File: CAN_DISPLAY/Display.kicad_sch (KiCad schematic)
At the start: 14 parts, among them J1 DISPLAY, J14 Display, J2 I2C Sensor 1, J3 I2C Sensor 2, U6 BME280

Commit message: PCB Fixes
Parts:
- added J16: BME280 Module, Connector_PinHeader_2.54mm:PinHeader_1x04_P2.54mm_Vertical, symbol Connector_Generic:Conn_01x04
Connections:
- net +3V3: now also J16.1 (Pin_1)
- net GND: now also J16.2 (Pin_2)
- net I2C_SCL: now also J16.3 (Pin_3)
- net I2C_SDA: now also J16.4 (Pin_4)
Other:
- moved on the sheet: C4, C5, J2, J3

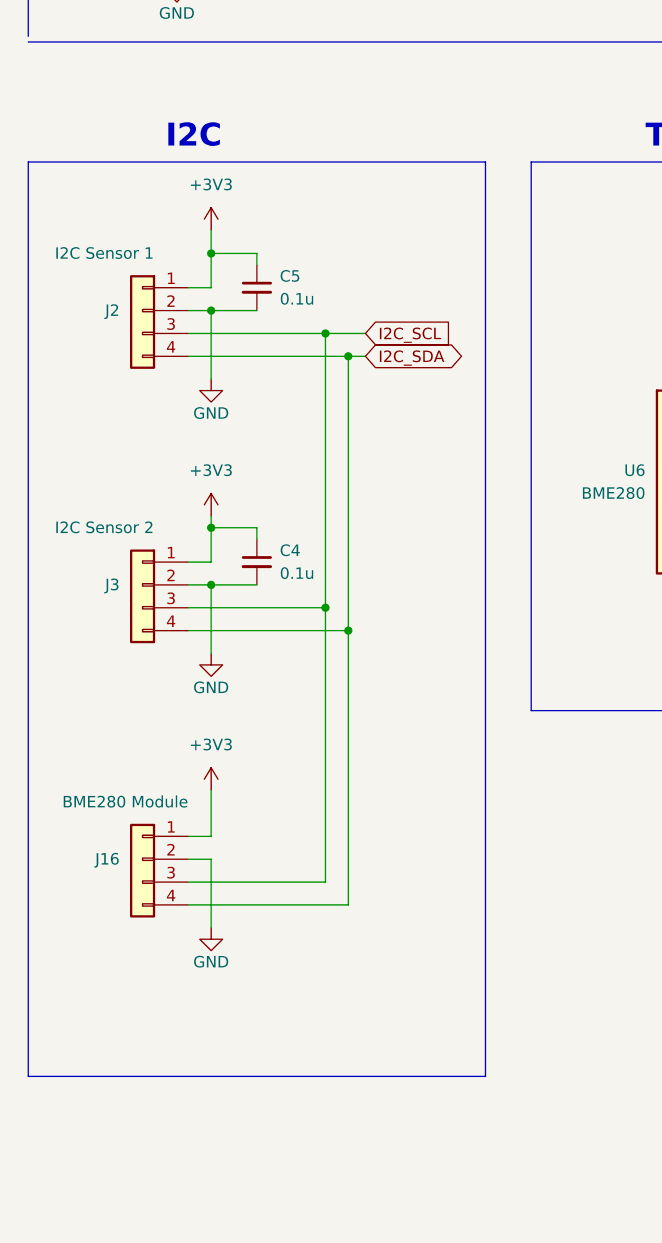
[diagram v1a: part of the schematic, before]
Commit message: Add Ambient Light
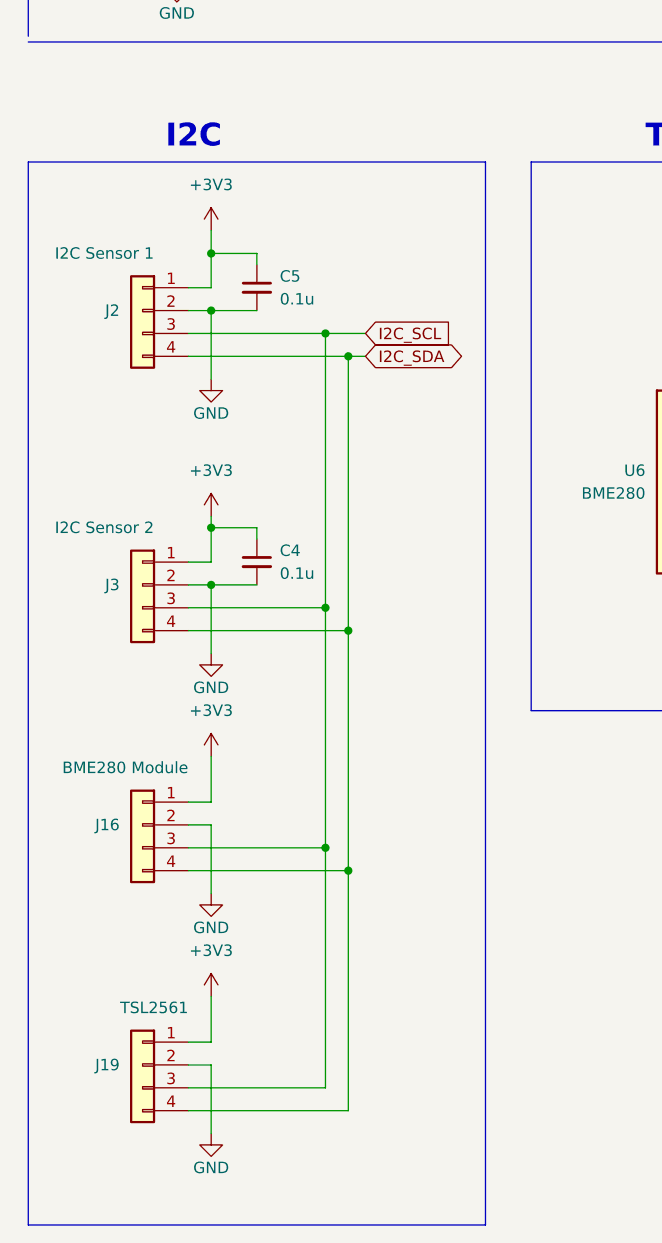
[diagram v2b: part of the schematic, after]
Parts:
- added J19: TSL2561, Connector_PinHeader_2.54mm:PinHeader_1x04_P2.54mm_Vertical, symbol Connector_Generic:Conn_01x04
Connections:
- net +3V3: now also J19.1 (Pin_1)
- net GND: now also J19.2 (Pin_2)
- net I2C_SCL: now also J19.3 (Pin_3)
- net I2C_SDA: now also J19.4 (Pin_4)
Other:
- moved on the sheet: J16
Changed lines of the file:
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@@
   (junction (at 46.355 41.91) (diameter 0) (color 0 0 0 0)
   )
+  (junction (at 54.61 153.67) (diameter 0) (color 0 0 0 0)
+  )
   (junction (at 67.945 28.575) (diameter 0) (color 0 0 0 0)
   )
@@
   )
   (junction (at 54.61 127) (diameter 0) (color 0 0 0 0)
+  )
+  (junction (at 52.07 151.13) (diameter 0) (color 0 0 0 0)
   )
   (no_connect (at 33.02 44.45))
@@
     (stroke (width 0) (type default))
   )
-  (wire (pts (xy 39.37 160.02) (xy 39.37 152.4))
+  (wire (pts (xy 39.37 156.21) (xy 39.37 148.59))
     (stroke (width 0) (type default))
   )
@@
     (stroke (width 0) (type default))
   )
+  (wire (pts (xy 36.83 172.72) (xy 39.37 172.72))
+    (stroke (width 0) (type default))
+  )
   (wire (pts (xy 101.6 93.98) (xy 96.52 93.98))
     (stroke (width 0) (type default))
   )
-  (wire (pts (xy 52.07 124.46) (xy 52.07 154.94))
+  (wire (pts (xy 52.07 124.46) (xy 52.07 151.13))
     (stroke (width 0) (type default))
   )
@@
     (stroke (width 0) (type default))
   )
+  (wire (pts (xy 36.83 177.8) (xy 52.07 177.8))
+    (stroke (width 0) (type default))
+  )
   (wire (pts (xy 52.705 39.37) (xy 45.085 39.37))
     (stroke (width 0) (type default))
@@
     (stroke (width 0) (type default))
   )
-  (wire (pts (xy 36.83 149.86) (xy 39.37 149.86))
+  (wire (pts (xy 36.83 146.05) (xy 39.37 146.05))
     (stroke (width 0) (type default))
   )
@@
     (stroke (width 0) (type default))
   )
+  (wire (pts (xy 39.37 182.88) (xy 39.37 175.26))
+    (stroke (width 0) (type default))
+  )
   (wire (pts (xy 54.61 127) (xy 54.61 96.52))
     (stroke (width 0) (type default))
@@
     (stroke (width 0) (type default))
   )
+  (wire (pts (xy 39.37 175.26) (xy 36.83 175.26))
+    (stroke (width 0) (type default))
+  )
   (wire (pts (xy 39.37 121.92) (xy 44.45 121.92))
     (stroke (width 0) (type default))
@@
     (stroke (width 0) (type default))
   )
-  (wire (pts (xy 54.61 157.48) (xy 54.61 127))
+  (wire (pts (xy 54.61 153.67) (xy 54.61 127))
     (stroke (width 0) (type default))
   )
@@
     (stroke (width 0) (type default))
   )
-  (wire (pts (xy 39.37 144.78) (xy 39.37 149.86))
+  (wire (pts (xy 39.37 140.97) (xy 39.37 146.05))
+    (stroke (width 0) (type default))
+  )
+  (wire (pts (xy 39.37 167.64) (xy 39.37 172.72))
     (stroke (width 0) (type default))
   )
@@
     (stroke (width 0) (type default))
   )
+  (wire (pts (xy 36.83 180.34) (xy 54.61 180.34))
+    (stroke (width 0) (type default))
+  )
   (wire (pts (xy 33.02 34.29) (xy 35.56 34.29))
     (stroke (width 0) (type default))
@@
     (stroke (width 0) (type default))
   )
-  (wire (pts (xy 36.83 157.48) (xy 54.61 157.48))
+  (wire (pts (xy 36.83 153.67) (xy 54.61 153.67))
     (stroke (width 0) (type default))
   )
@@
     (stroke (width 0) (type default))
   )
-  (wire (pts (xy 36.83 154.94) (xy 52.07 154.94))
+  (wire (pts (xy 36.83 151.13) (xy 52.07 151.13))
     (stroke (width 0) (type default))
   )
@@
     (stroke (width 0) (type default))
   )
+  (wire (pts (xy 54.61 180.34) (xy 54.61 153.67))
+    (stroke (width 0) (type default))
+  )
   (wire (pts (xy 119.38 118.11) (xy 114.3 118.11))
     (stroke (width 0) (type default))
   )
-  (wire (pts (xy 39.37 152.4) (xy 36.83 152.4))
+  (wire (pts (xy 39.37 148.59) (xy 36.83 148.59))
+    (stroke (width 0) (type default))
+  )
+  (wire (pts (xy 52.07 151.13) (xy 52.07 177.8))
     (stroke (width 0) (type default))
   )
@@
     (fill (type none))
   )
-  (rectangle (start 19.05 74.93) (end 69.85 176.53)
+  (rectangle (start 19.05 74.93) (end 69.85 193.04)
     (stroke (width 0) (type default))
     (fill (type none))
@@
     )
   )
-  (symbol (lib_id "power:GND") (at 39.37 160.02 0) (mirror y) (unit 1)
-    (in_bom yes) (on_board yes) (dnp no)
-    (property "Reference" "#PWR086" (at 39.37 166.37 0)
-      (effects (font (size 1.27 1.27)) hide)
-    )
-    (property "Value" "GND" (at 39.37 163.83 0)
-      (effects (font (size 1.27 1.27)))
-    )
-    (property "Footprint" "" (at 39.37 160.02 0)
-      (effects (font (size 1.27 1.27)) hide)
-    )
-    (property "Datasheet" "" (at 39.37 160.02 0)
+  (symbol (lib_id "power:GND") (at 39.37 156.21 0) (mirror y) (unit 1)
+    (in_bom yes) (on_board yes) (dnp no)
+    (property "Reference" "#PWR086" (at 39.37 162.56 0)
+      (effects (font (size 1.27 1.27)) hide)
+    )
+    (property "Value" "GND" (at 39.37 160.02 0)
+      (effects (font (size 1.27 1.27)))
+    )
+    (property "Footprint" "" (at 39.37 156.21 0)
+      (effects (font (size 1.27 1.27)) hide)
+    )
+    (property "Datasheet" "" (at 39.37 156.21 0)
       (effects (font (size 1.27 1.27)) hide)
     )
@@
     )
   )
-  (symbol (lib_id "power:+3V3") (at 39.37 144.78 0) (unit 1)
+  (symbol (lib_id "power:+3V3") (at 39.37 140.97 0) (unit 1)
     (in_bom yes) (on_board yes) (dnp no) (fields_autoplaced)
-    (property "Reference" "#PWR085" (at 39.37 148.59 0)
-      (effects (font (size 1.27 1.27)) hide)
-    )
-    (property "Value" "+3V3" (at 39.37 139.7 0)
-      (effects (font (size 1.27 1.27)))
-    )
-    (property "Footprint" "" (at 39.37 144.78 0)
-      (effects (font (size 1.27 1.27)) hide)
-    )
-    (property "Datasheet" "" (at 39.37 144.78 0)
+    (property "Reference" "#PWR085" (at 39.37 144.78 0)
+      (effects (font (size 1.27 1.27)) hide)
+    )
+    (property "Value" "+3V3" (at 39.37 135.89 0)
+      (effects (font (size 1.27 1.27)))
+    )
+    (property "Footprint" "" (at 39.37 140.97 0)
+      (effects (font (size 1.27 1.27)) hide)
+    )
+    (property "Datasheet" "" (at 39.37 140.97 0)
       (effects (font (size 1.27 1.27)) hide)
     )
@@
     )
   )
-  (symbol (lib_id "Connector_Generic:Conn_01x04") (at 31.75 152.4 0) (mirror y) (unit 1)
-    (in_bom yes) (on_board yes) (dnp no)
-    (property "Reference" "J16" (at 29.21 152.4 0)
-      (effects (font (size 1.27 1.27)) (justify left))
-    )
-    (property "Value" "BME280 Module" (at 36.83 146.05 0)
-      (effects (font (size 1.27 1.27)) (justify left))
-    )
-    (property "Footprint" "Connector_PinHeader_2.54mm:PinHeader_1x04_P2.54mm_Vertical" (at 31.75 152.4 0)
-      (effects (font (size 1.27 1.27)) hide)
-    )
-    (property "Datasheet" "~" (at 31.75 152.4 0)
+  (symbol (lib_id "Connector_Generic:Conn_01x04") (at 31.75 148.59 0) (mirror y) (unit 1)
+    (in_bom yes) (on_board yes) (dnp no)
+    (property "Reference" "J16" (at 29.21 148.59 0)
+      (effects (font (size 1.27 1.27)) (justify left))
+    )
+    (property "Value" "BME280 Module" (at 36.83 142.24 0)
+      (effects (font (size 1.27 1.27)) (justify left))
+    )
+    (property "Footprint" "Connector_PinHeader_2.54mm:PinHeader_1x04_P2.54mm_Vertical" (at 31.75 148.59 0)
+      (effects (font (size 1.27 1.27)) hide)
+    )
+    (property "Datasheet" "~" (at 31.75 148.59 0)
       (effects (font (size 1.27 1.27)) hide)
     )
@@
     )
   )
+  (symbol (lib_id "Connector_Generic:Conn_01x04") (at 31.75 175.26 0) (mirror y) (unit 1)
+    (in_bom yes) (on_board yes) (dnp no)
+    (property "Reference" "J19" (at 29.21 175.26 0)
+      (effects (font (size 1.27 1.27)) (justify left))
+    )
+    (property "Value" "TSL2561" (at 36.83 168.91 0)
+      (effects (font (size 1.27 1.27)) (justify left))
+    )
+    (property "Footprint" "Connector_PinHeader_2.54mm:PinHeader_1x04_P2.54mm_Vertical" (at 31.75 175.26 0)
+      (effects (font (size 1.27 1.27)) hide)
+    )
+    (property "Datasheet" "~" (at 31.75 175.26 0)
+      (effects (font (size 1.27 1.27)) hide)
+    )
+    (pin "1")
+    (pin "2")
+    (pin "3")
+    (pin "4")
+    (instances
+      (project "CAN_DISPLAY"
+        (path "/7b7bcc60-3b35-483b-8f75-db7ec854d7bb/ea039cf5-2d2d-4347-8210-9e077b57066c"
+          (reference "J19") (unit 1)
+        )
+      )
+    )
+  )
   (symbol (lib_id "power:+3V3") (at 39.37 114.3 0) (unit 1)
     (in_bom yes) (on_board yes) (dnp no) (fields_autoplaced)
@@
     )
   )
+  (symbol (lib_id "power:+3V3") (at 39.37 167.64 0) (unit 1)
+    (in_bom yes) (on_board yes) (dnp no) (fields_autoplaced)
+    (property "Reference" "#PWR091" (at 39.37 171.45 0)
+      (effects (font (size 1.27 1.27)) hide)
+    )
+    (property "Value" "+3V3" (at 39.37 162.56 0)
+      (effects (font (size 1.27 1.27)))
+    )
+    (property "Footprint" "" (at 39.37 167.64 0)
+      (effects (font (size 1.27 1.27)) hide)
+    )
+    (property "Datasheet" "" (at 39.37 167.64 0)
+      (effects (font (size 1.27 1.27)) hide)
+    )
+    (pin "1")
+    (instances
+      (project "CAN_DISPLAY"
+        (path "/7b7bcc60-3b35-483b-8f75-db7ec854d7bb/ea039cf5-2d2d-4347-8210-9e077b57066c"
+          (reference "#PWR091") (unit 1)
+        )
+      )
+    )
+  )
   (symbol (lib_id "Device:C_Polarized_Small") (at 97.155 38.735 0) (unit 1)
     (in_bom yes) (on_board yes) (dnp no)
@@
         )
       )
+    )
+  )
+  (symbol (lib_id "power:GND") (at 39.37 182.88 0) (mirror y) (unit 1)
+    (in_bom yes) (on_board yes) (dnp no)
+    (property "Reference" "#PWR092" (at 39.37 189.23 0)
+      (effects (font (size 1.27 1.27)) hide)
+    )
+    (property "Value" "GND" (at 39.37 186.69 0)
+      (effects (font (size 1.27 1.27)))
+    )
+    (property "Footprint" "" (at 39.37 182.88 0)
+      (effects (font (size 1.27 1.27)) hide)
+    )
+    (property "Datasheet" "" (at 39.37 182.88 0)
+      (effects (font (size 1.27 1.27)) hide)
+    )
+    (pin "1")
+    (instances
+      (project "CAN_DISPLAY"
+        (path "/7b7bcc60-3b35-483b-8f75-db7ec854d7bb/ea039cf5-2d2d-4347-8210-9e077b57066c"
+          (reference "#PWR092") (unit 1)
+        )
+      )
